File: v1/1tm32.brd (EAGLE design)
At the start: 50.8 x 50.8 mm, 45 parts, among them IC1 STM32L412RBT6P, IC2 BGM240PA32VNN3, J2 10118192-0001LF, J3 FTSH-105-01-L-D, J4 20021321-00020C4LF, SW1 LL3301FF065QJ, U2 LD39050PU33R, Y1 8MHz, Y2 32.7KHz

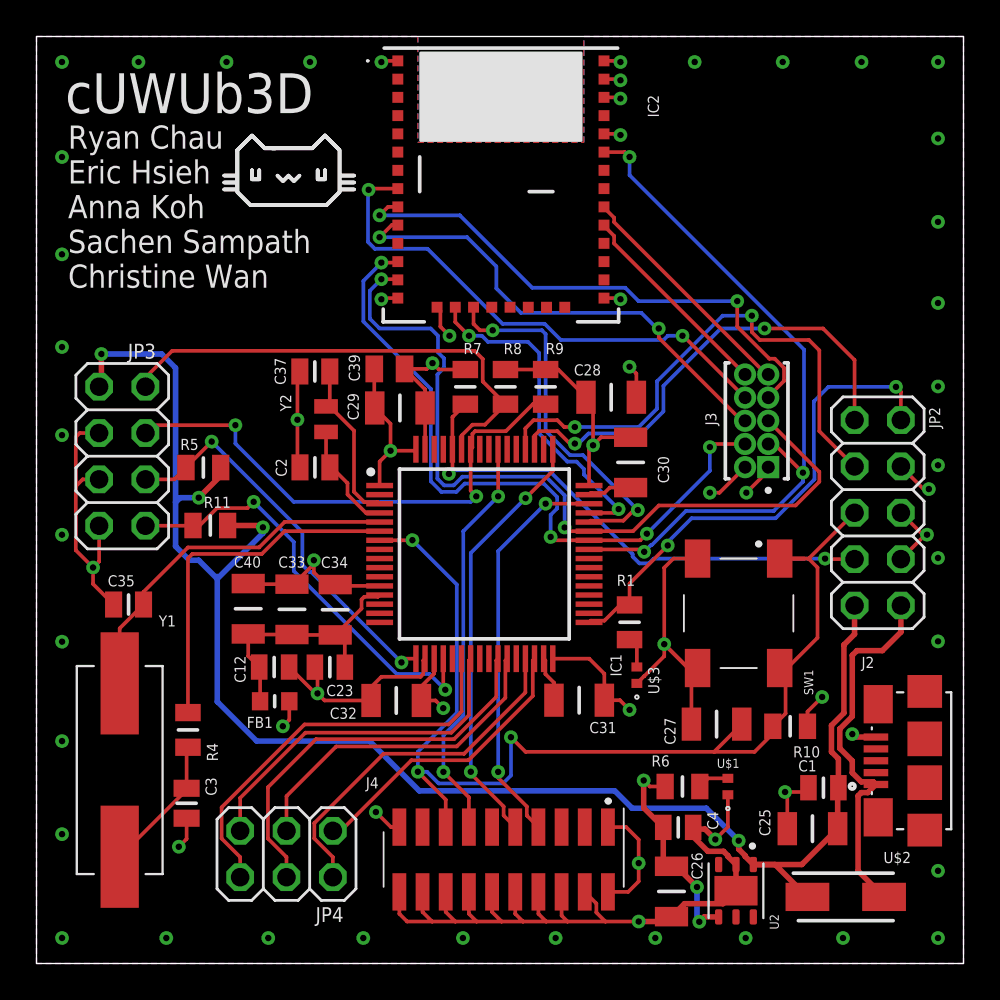
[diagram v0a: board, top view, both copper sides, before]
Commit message: updated the Schottky diode to RBR1L30ATE25
datasheet: https://www.mouser.com/datasheet/2/348/ROHM_S_A0008995718_1-2562906.pdf
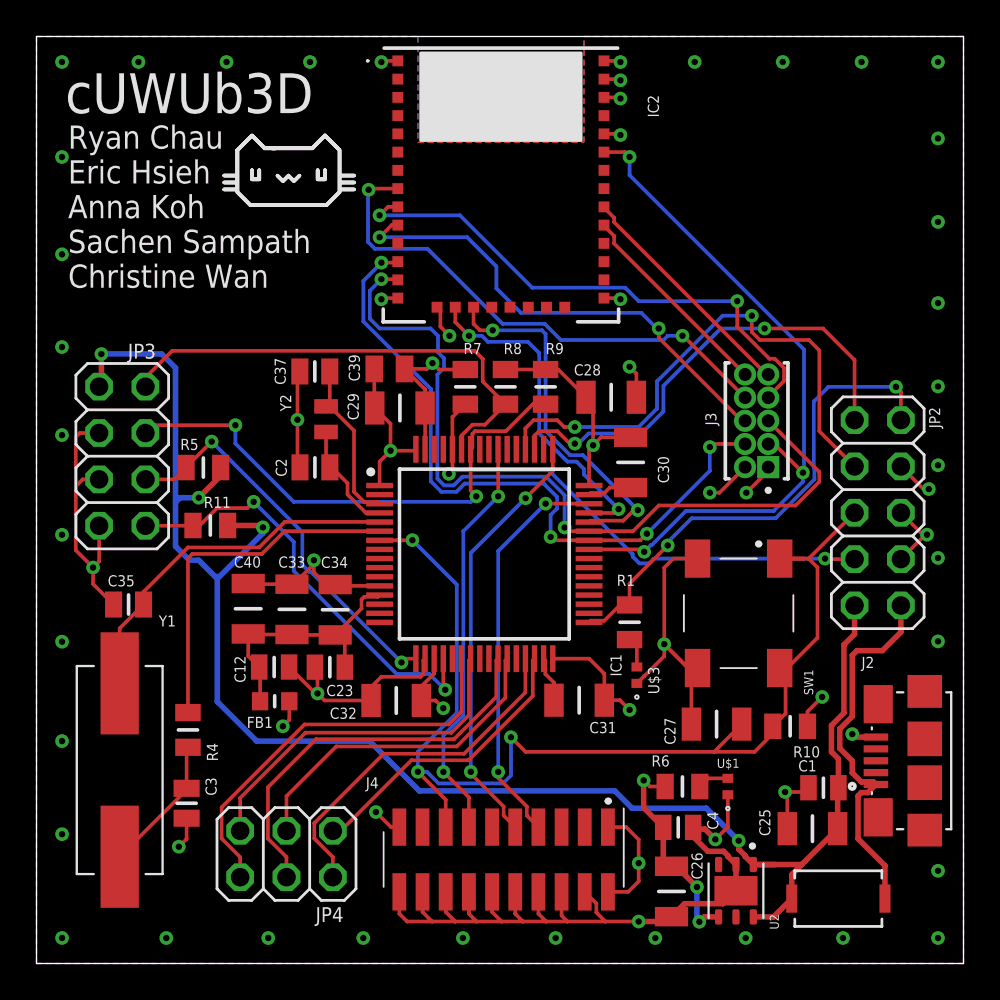
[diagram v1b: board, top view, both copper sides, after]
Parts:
- U$2: value STPS1L30A -> RBR1L30ATE25; device ce-capstone:DIOM5226X223N -> RBR1L30ATE25(scho_diode):DIO_RBR1L30_ROM
- moved U$2 0.42 mm to (43.9, 3.56), turned to 180 degrees
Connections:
- net 5V: now also U$2.2; no longer U$2.1
- net 5V_IN: now also U$2.1; no longer U$2.2
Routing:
- net 5V: track 90.7 -> 92.8 mm
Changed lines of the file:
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@@
 <vertex x="21" y="44.2"/>
-<vertex x="21" y="42.3"/>
 <vertex x="21" y="42.3"/>
 </polygon>
@@
 <vertex x="27" y="42.3"/>
 <vertex x="28.3" y="42.3"/>
-<vertex x="27" y="42.3"/>
 </polygon>
 <polygon width="0.2032" layer="21">
@@
 <attribute name="PRICE" value="None" x="88.687" y="52.877" size="1.778" layer="27" rot="R90" display="off"/>
 </element>
-<element name="U$2" library="ce-capstone" package="DIOM5226X223N" value="STPS1L30A" x="44.347" y="3.649" smashed="yes">
-<attribute name="NAME" x="47.168" y="5.808" size="0.6096" layer="25" align="center"/>
-</element>
 <element name="U2" library="ce-capstone" package="SON95P300X300X100-7N" value="LD39050PU33R" x="38.332" y="3.988" smashed="yes" rot="R270">
 <attribute name="AVAILABILITY" value="Unavailable" x="1.502" y="-39.192" size="1.778" layer="27" rot="R270" display="off"/>
@@
 <attribute name="MOUSER_PRICE-STOCK" value="https://www.mouser.co.uk/ProductDetail/YAGEO/RC0805JR-0710KL?qs=ZFGQJeMQzF5q%2Fp77vM%2FrVQ%3D%3D" x="9.525" y="24.003" size="1.778" layer="27" rot="R180" display="off"/>
 <attribute name="NAME" x="9.906" y="25.273" size="0.6096" layer="25" align="center"/>
+</element>
+<element name="U$2" library="RBR1L30ATE25(scho_diode)" package="DIO_RBR1L30_ROM" value="RBR1L30ATE25" x="43.942" y="3.556" smashed="yes" rot="R180">
+<attribute name="COPYRIGHT" value="Copyright (C) 2023 Ultra Librarian. All rights reserved." x="43.942" y="3.556" size="1.778" layer="27" rot="R180" display="off"/>
+<attribute name="DIGI-KEY_PART_NUMBER_1" value="RBR1L30ATE25CT-ND" x="43.942" y="3.556" size="1.778" layer="27" rot="R180" display="off"/>
+<attribute name="DIGI-KEY_PART_NUMBER_2" value="RBR1L30ATE25DKR-ND" x="43.942" y="3.556" size="1.778" layer="27" rot="R180" display="off"/>
+<attribute name="DIGI-KEY_PART_NUMBER_3" value="RBR1L30ATE25TR-ND" x="43.942" y="3.556" size="1.778" layer="27" rot="R180" display="off"/>
+<attribute name="MANUFACTURER_PART_NUMBER" value="RBR1L30ATE25" x="43.942" y="3.556" size="1.778" layer="27" rot="R180" display="off"/>
+<attribute name="MFR_NAME" value="ROHM Semiconductor" x="43.942" y="3.556" size="1.778" layer="27" rot="R180" display="off"/>
+<attribute name="NAME" x="47.498" y="2.0574" size="0.5" layer="27" ratio="6" rot="SR90"/>
 </element>
 </elements>
@@
 </signal>
 <signal name="5V_IN">
-<contactref element="U$2" pad="2"/>
 <contactref element="J2" pad="1"/>
 <contactref element="JP2" pad="10"/>
-<wire x1="45.19975" y1="9.3648" x2="45.0212" y2="9.18625" width="0.3048" layer="1"/>
 <wire x1="46.001" y1="9.81" x2="45.5558" y2="9.3648" width="0.3048" layer="1"/>
 <wire x1="45.5558" y1="9.3648" x2="45.19975" y2="9.3648" width="0.3048" layer="1"/>
-<wire x1="45.0212" y1="9.18625" x2="45.0212" y2="5.0748" width="0.3048" layer="1"/>
-<wire x1="45.0212" y1="5.0748" x2="46.447" y2="3.649" width="0.3048" layer="1"/>
 <wire x1="47.37" y1="19.62" x2="47.37" y2="18.16" width="0.3048" layer="1"/>
 <wire x1="45.19975" y1="9.9552" x2="45.8558" y2="9.9552" width="0.3048" layer="1"/>
@@
 <wire x1="44.704" y1="16.891" x2="44.958" y2="17.145" width="0.3048" layer="1"/>
 <wire x1="44.958" y1="17.145" x2="46.355" y2="17.145" width="0.3048" layer="1"/>
+<contactref element="U$2" pad="1"/>
+<wire x1="45.19975" y1="9.3648" x2="45.0212" y2="9.18625" width="0.3048" layer="1"/>
+<wire x1="45.0212" y1="9.18625" x2="45.0212" y2="6.83375" width="0.3048" layer="1"/>
+<wire x1="46.4947" y1="5.36025" x2="46.4947" y2="3.556" width="0.3048" layer="1"/>
+<wire x1="45.0212" y1="6.83375" x2="46.4947" y2="5.36025" width="0.3048" layer="1"/>
 </signal>
 <signal name="5V">
 <contactref element="U2" pad="6"/>
-<contactref element="U$2" pad="1"/>
 <contactref element="U2" pad="1"/>
 <contactref element="C1" pad="2"/>
@@
 <contactref element="JP3" pad="1"/>
 <wire x1="39.282" y1="5.423" x2="40.473" y2="5.423" width="0.3048" layer="1"/>
-<wire x1="40.473" y1="5.423" x2="42.247" y2="3.649" width="0.3048" layer="1"/>
 <wire x1="39.282" y1="5.423" x2="41.939" y2="5.423" width="0.3048" layer="1"/>
-<wire x1="41.939" y1="5.423" x2="43.904" y2="7.388" width="0.3048" layer="1"/>
+<wire x1="41.939" y1="5.423" x2="42.134" y2="5.618" width="0.3048" layer="1"/>
+<wire x1="42.134" y1="5.618" x2="43.904" y2="7.388" width="0.3048" layer="1"/>
 <wire x1="43.904" y1="7.388" x2="43.904" y2="9.592" width="0.3048" layer="1"/>
 <wire x1="43.904" y1="9.592" x2="43.944" y2="9.632" width="0.3048" layer="1"/>
@@
 <wire x1="10.475" y1="24.003" x2="12.30293125" y2="24.003" width="0.3048" layer="1"/>
 <wire x1="12.30293125" y1="24.003" x2="12.40593125" y2="23.9" width="0.3048" layer="1"/>
-<wire x1="39.282" y1="5.423" x2="39.282" y2="2.553" width="0" layer="19" extent="1-1"/>
+<contactref element="U$2" pad="2"/>
+<wire x1="39.282" y1="2.553" x2="40.3863" y2="2.553" width="0.3048" layer="1"/>
+<wire x1="40.3863" y1="2.553" x2="41.3893" y2="3.556" width="0.3048" layer="1"/>
+<wire x1="41.3893" y1="3.556" x2="41.3893" y2="4.8733" width="0.3048" layer="1"/>
+<wire x1="41.3893" y1="4.8733" x2="41.939" y2="5.423" width="0.3048" layer="1"/>
 </signal>
 <signal name="N$5">

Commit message: changed errors
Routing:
- net GND: track 136.7 -> 144.1 mm, vias 55 -> 56
- net 3V3: track 61.3 -> 63.8 mm
- net NRST: track 62.7 -> 61.3 mm
- net 5V: track 92.8 -> 91.5 mm
